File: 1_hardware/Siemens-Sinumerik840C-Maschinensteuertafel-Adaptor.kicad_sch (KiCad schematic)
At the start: 23 parts, among them U1 STM32F103C8T6, U2 AP22652AW6-7, U3 LD1117S33CTR

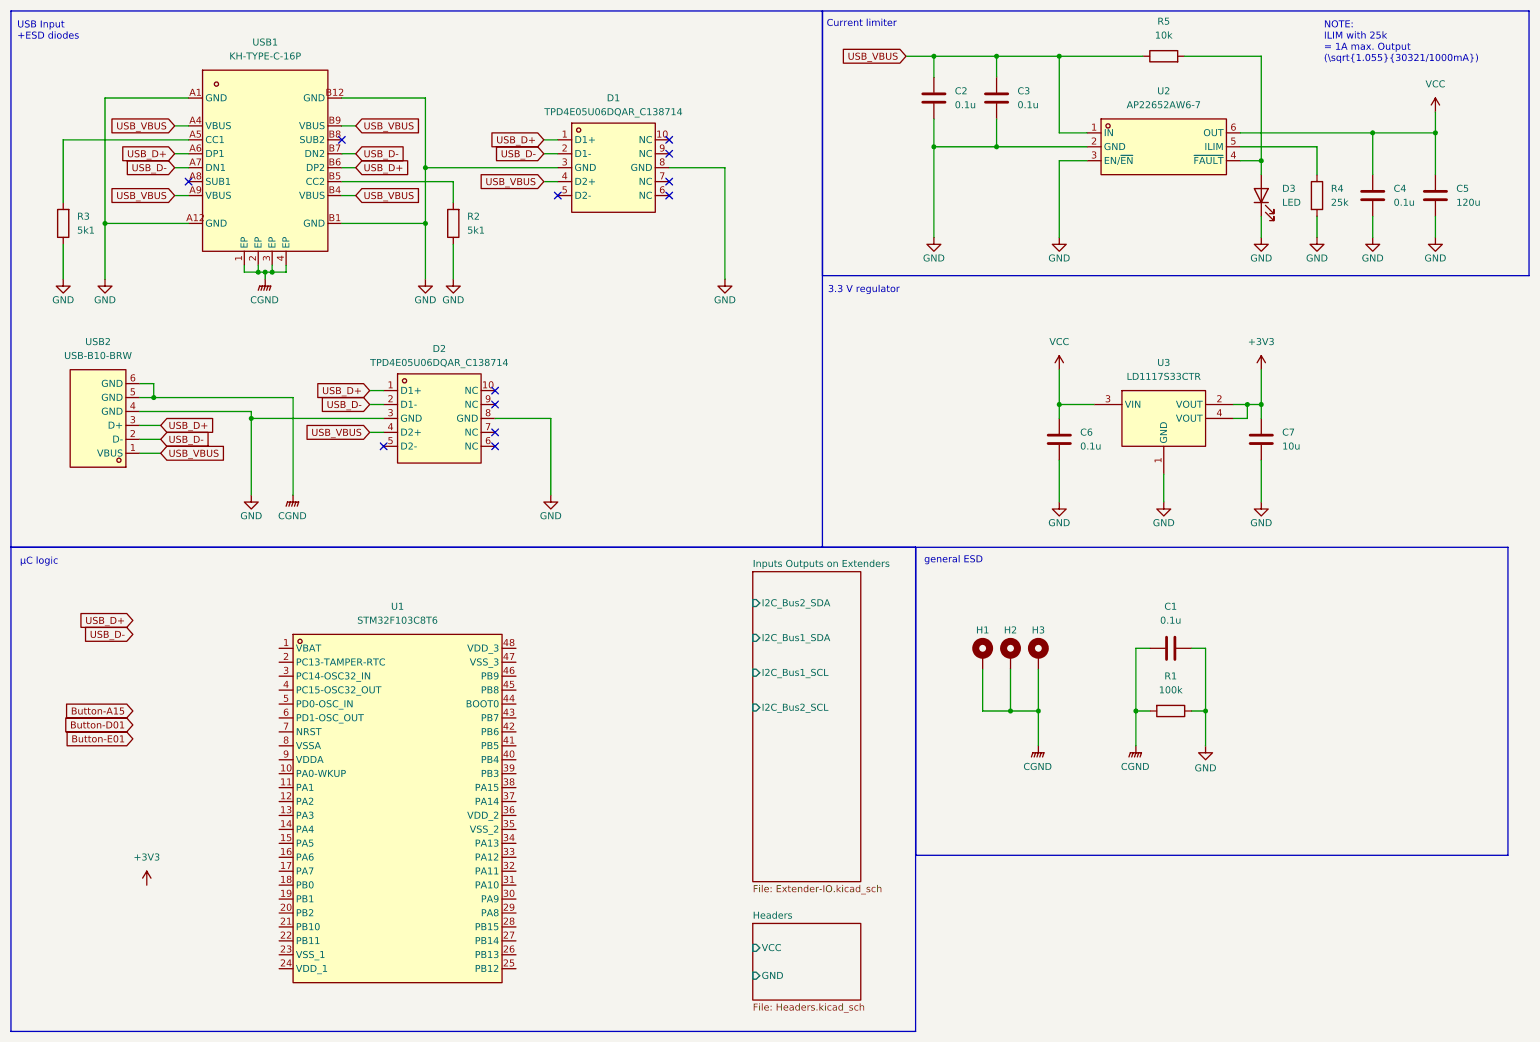
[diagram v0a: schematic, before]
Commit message: finished most of schematic, init STM32 program
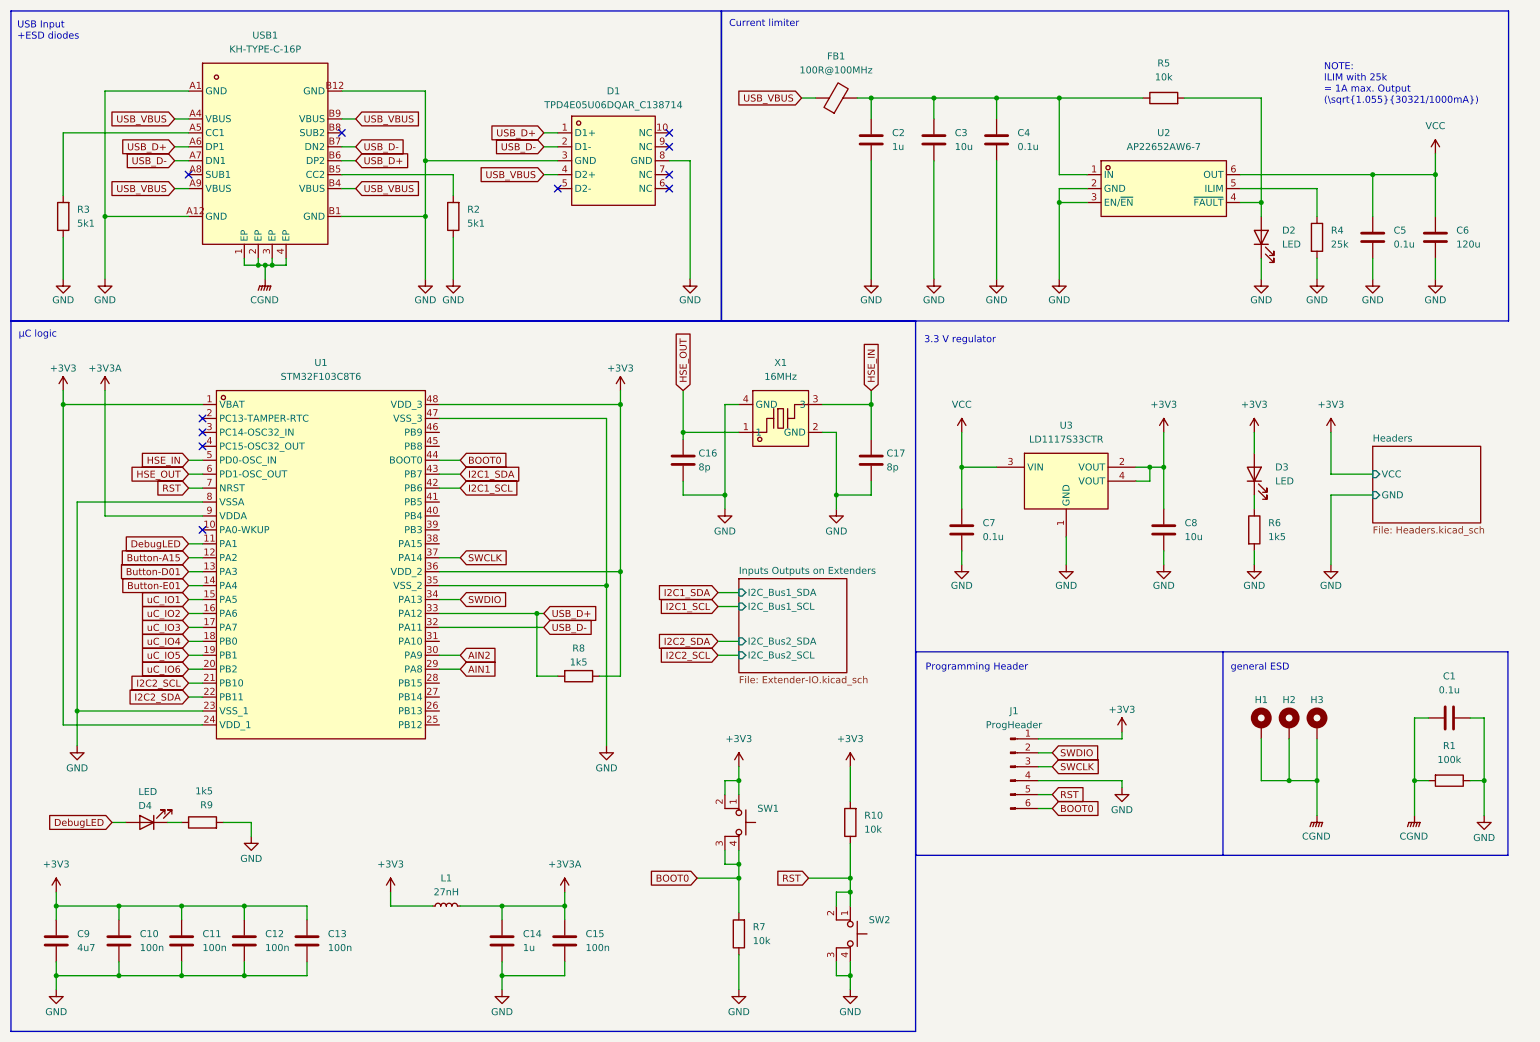
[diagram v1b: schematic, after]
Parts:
- removed D2: TPD4E05U06DQAR_C138714, easyeda2kicad:USON-10_L2.5-W1.0-P0.50-BL, symbol easyeda2kicad:TPD4E05U06DQAR_C138714
- removed USB2: USB-B10-BRW, easyeda2kicad:USB-B-TH_USB-B10-BRW, symbol easyeda2kicad:USB-B10-BRW
- added C10, C11, C12, C13, C15: 100n, Capacitor_SMD:C_0603_1608Metric, symbol Device:C
- added C14, C2: 1u, Capacitor_SMD:C_0603_1608Metric, symbol Device:C
- added C16, C17: 8p, Capacitor_SMD:C_0603_1608Metric, symbol Device:C
- added C9: 4u7, Capacitor_SMD:C_0603_1608Metric, symbol Device:C
- added D3, D4: LED, LED_SMD:LED_0603_1608Metric, symbol Device:LED
- added FB1: 100R@100MHz, easyeda2kicad:L0603, symbol Device:FerriteBead
- added J1: ProgHeader, easyeda2kicad:HDR-SMD_6P-P2.54-V-M-LS4.8_R2, symbol Connector:Conn_01x06_Pin
- added L1: 27nH, Inductor_SMD:L_0603_1608Metric, symbol Device:L_Small
- added R10, R7: 10k, Resistor_SMD:R_0603_1608Metric, symbol Device:R
- added R6, R8, R9: 1k5, Resistor_SMD:R_0603_1608Metric, symbol Device:R
- added SW1, SW2: TS-1187A-B-A-B, easyeda2kicad:SW-SMD_4P-L5.1-W5.1-P3.70-LS6.5-TL-2, symbol Switch:SW_MEC_5E
- added X1: 16MHz, easyeda2kicad:CRYSTAL-SMD_4P-L3.2-W2.5-BL_SIT8008BI, symbol easyeda2kicad:TZ0233A
- C3: renamed from C2; value 0.1u -> 10u
- renumbered C3 to C4, C4 to C5, C5 to C6, C6 to C7, C7 to C8, D3 to D2
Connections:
- net +3V3: now also U1.1 (VBAT), U1.24 (VDD_1), U1.36 (VDD_2), U1.48 (VDD_3), C10.2, C11.2, C12.2, C13.2, C9.2, D3.2 (A), J1.1 (Pin_1), L1.1, R10.2, R8.1, SW1.1, SW1.2
- net Button-A15: now also U1.12 (PA2)
- net Button-D01: now also U1.13 (PA3)
- net Button-E01: now also U1.14 (PA4)
- net GND: now also U1.23 (VSS_1), U1.35 (VSS_2), U1.47 (VSS_3), U1.8 (VSSA), C10.1, C11.1, C12.1, C13.1, C14.1, C15.1, C16.1, C17.1, C2.1, C9.1, J1.4 (Pin_4), R6.2, R7.1, R9.2, SW2.3 (K), SW2.4 (A), X1.2 (GND), X1.4 (GND)
- net USB_D+: now also U1.33 (PA12), R8.2
- net USB_D-: now also U1.32 (PA11)
- net USB_VBUS: now also FB1.1; no longer C3.2, C4.2, R5.1, U2.1 (IN)
- net DebugLED: now reaches U1.11 (PA1)
- net DebugLED: now also D4.2 (A)
- net uC_IO1: now reaches U1.15 (PA5)
- net uC_IO2: now reaches U1.16 (PA6)
- net uC_IO3: now reaches U1.17 (PA7)
- net uC_IO4: now reaches U1.18 (PB0)
- net uC_IO5: now reaches U1.19 (PB1)
- net uC_IO6: now reaches U1.20 (PB2)
- net I2C2_SCL: now reaches U1.21 (PB10)
- net I2C2_SDA: now reaches U1.22 (PB11)
- net AIN1: now reaches U1.29 (PA8)
- net AIN2: now reaches U1.30 (PA9)
- net SWDIO: now reaches U1.34 (PA13)
- net SWDIO: now also J1.2 (Pin_2)
- net SWCLK: now reaches U1.37 (PA14)
- net SWCLK: now also J1.3 (Pin_3)
- net I2C1_SCL: now reaches U1.42 (PB6)
- net I2C1_SDA: now reaches U1.43 (PB7)
- net BOOT0: now reaches U1.44 (BOOT0)
- net BOOT0: now also J1.6 (Pin_6), R7.2, SW1.3 (K), SW1.4 (A)
- net HSE_IN: now reaches U1.5 (PD0-OSC_IN)
- net HSE_IN: now also C17.2, X1.3
- net HSE_OUT: now reaches U1.6 (PD1-OSC_OUT)
- net HSE_OUT: now also C16.2, X1.1
- net RST: now reaches U1.7 (NRST)
- net RST: now also J1.5 (Pin_5), R10.1, SW2.1, SW2.2
- net +3V3A: now reaches U1.9 (VDDA)
- net +3V3A: now also C14.2, C15.2, L1.2
- new net: D3.1 (K), R6.1
- new net: C2.2, C3.2, C4.2, FB1.2, R5.1, U2.1 (IN)
- new net: D4.1 (K), R9.1
- no-connect marks 12 -> 11
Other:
- note added: "Programming Header"
- moved on the sheet: C1, C3, C4, C5, C6, C7, C8, D1, D2, H1, H2, H3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

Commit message: finished schematics and board
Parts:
- added R11, R12, R13, R14, R15, R16, R17, R18: 10k, Resistor_SMD:R_0603_1608Metric, symbol Device:R
- added R19, R20, R21, R22: 1k5, Resistor_SMD:R_0603_1608Metric, symbol Device:R
- C1: footprint Capacitor_SMD:C_0805_2012Metric -> Capacitor_SMD:C_1206_3216Metric
- H1, H2, H3: footprint MountingHole:MountingHole_3.2mm_M3_DIN965_Pad_TopBottom -> MountingHole:MountingHole_3.2mm_M3_DIN965_Pad
- R1: footprint Resistor_SMD:R_0805_2012Metric -> Resistor_SMD:R_1206_3216Metric
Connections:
- net +3V3: now also R11.2, R12.2, R13.2, R14.2, R15.2, R16.2, R17.2, R18.2, R19.2, R20.2, R21.2, R22.2
- net CGND: now also C1.2, H1.1, H2.1, H3.1; no longer C1.1, H1.MP, H2.MP, H3.MP
- net GND: now also C1.1; no longer C1.2
- net I2C1_SCL: now also R20.1
- net I2C1_SDA: now also R19.1
- net I2C2_SCL: now also R22.1
- net I2C2_SDA: now also R21.1
- net USB_D+: now also D1.10 (NC)
- net USB_D-: now also D1.9 (NC)
- net USB_VBUS: now also D1.7 (NC)
- net EXP_INT4: now reaches U1.39 (PB3)
- net EXP_INT4: now also R14.1
- net EXP_INT5: now reaches U1.40 (PB4)
- net EXP_INT5: now also R15.1
- net EXP_INT6: now reaches U1.41 (PB5)
- net EXP_INT6: now also R16.1
- net EXP_INT7: now reaches U1.45 (PB8)
- net EXP_INT7: now also R17.1
- net EXP_INT8: now reaches U1.46 (PB9)
- net EXP_INT8: now also R18.1
- net Button-A15 renamed Button-~{A15}
- net Button-D01 renamed Button-~{D01}
- net Button-E01 renamed Button-~{E01}
- net uC_IO1: no longer names the net of U1.15 (PA5)
- net uC_IO2: no longer names the net of U1.16 (PA6)
- net uC_IO3: no longer names the net of U1.17 (PA7)
- net uC_IO4 renamed EXP_INT1
- net EXP_INT1: now also R11.1
- net uC_IO5 renamed EXP_INT2
- net EXP_INT2: now also R12.1
- net uC_IO6 renamed EXP_INT3
- net EXP_INT3: now also R13.1
- no-connect marks 11 -> 17
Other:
- sheet Inputs Outputs on Extenders renamed IO Expander
- sheet IO Expander ports: added EXP_INT1, EXP_INT2, EXP_INT3, EXP_INT4, EXP_INT5, EXP_INT6, EXP_INT7, EXP_INT8; removed none
- note added: "Programming Header/ Debug"
- note removed: "Programming Header"
- moved on the sheet: C1, C10, C11, C12, C13, C14, C15, C16, C17, C7, C8, C9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

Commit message: changed from STM32F103C8 over to STM32L151C8 changed controller pinout, minor tweaks in board design, added labels and debug pads
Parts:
- removed R8: 1k5, Resistor_SMD:R_0603_1608Metric, symbol Device:R
- removed U1: STM32F103C8T6, easyeda2kicad:LQFP-48_L7.0-W7.0-P0.50-LS9.0-BL, symbol easyeda2kicad:STM32F103C8T6
- added R2: 100k, Resistor_SMD:R_2512_6332Metric, symbol Device:R
- added R23: 1k5, Resistor_SMD:R_0603_1608Metric, symbol Device:R
- added TP1: JTDO-TraceSWO, TestPoint:TestPoint_Pad_D1.0mm, symbol Connector:TestPoint
- added TP2: JTDI, TestPoint:TestPoint_Pad_D1.0mm, symbol Connector:TestPoint
- added TP3: JTCK-SWCLK, TestPoint:TestPoint_Pad_D1.0mm, symbol Connector:TestPoint
- added TP4: JTMS-SWDIO, TestPoint:TestPoint_Pad_D1.0mm, symbol Connector:TestPoint
- added TP5: RESET, TestPoint:TestPoint_Pad_D1.0mm, symbol Connector:TestPoint
- added TP6: GND, TestPoint:TestPoint_Pad_D1.0mm, symbol Connector:TestPoint
- added U1: STM32L151C8T6, easyeda2kicad:LQFP-48_L7.0-W7.0-P0.50-LS9.0-BL, symbol easyeda2kicad:STM32L151C8T6
- C1: footprint Capacitor_SMD:C_1206_3216Metric -> Capacitor_SMD:C_2220_5750Metric
- R1: footprint Resistor_SMD:R_1206_3216Metric -> Resistor_SMD:R_2512_6332Metric
- R10: renamed from R9; value 1k5 -> 470
- R5: value 10k -> 680
- R7: renamed from R6; value 1k5 -> 470
- renumbered R2 to R4, R4 to R6, R7 to R8, R10 to R9
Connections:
- net +3V3: now also R23.1, U1.1 (VLCD), U1.24 (VDD), U1.36 (VDD), U1.48 (VDD)
- net +3V3A: now also U1.9 (VDDA)
- net AIN1: now also U1.11 (PA1)
- net AIN2: now also U1.12 (PA2)
- net BOOT0: now also U1.44 (BOOT0); no longer J1.6 (Pin_6)
- net Button-~{A15}: now also U1.18 (PB0)
- net Button-~{D01}: now also U1.19 (PB1)
- net Button-~{E01}: now also U1.20 (PB2)
- net CGND: now also R2.2
- net DebugLED: now also U1.13 (PA3)
- net EXP_INT1: now also U1.40 (PB4)
- net EXP_INT2: now also U1.41 (PB5)
- net EXP_INT3: now also U1.45 (PB8)
- net EXP_INT4: now also U1.46 (PB9)
- net EXP_INT5: now also U1.25 (PB12)
- net EXP_INT6: now also U1.26 (PB13)
- net EXP_INT7: now also U1.27 (PB14)
- net EXP_INT8: now also U1.28 (PB15)
- net GND: now also R2.1, TP6.1, U1.23 (VSS), U1.35 (VSS), U1.47 (VSS), U1.8 (VSSA)
- net HSE_IN: now also U1.5 (PH0-OSC/IN)
- net HSE_OUT: now also U1.6 (PH1-OSC/OUT)
- net I2C1_SCL: now also U1.42 (PB6)
- net I2C1_SDA: now also U1.43 (PB7)
- net I2C2_SCL: now also U1.21 (PB10)
- net I2C2_SDA: now also U1.22 (PB11)
- net RST: now also TP5.1, U1.7 (NRST)
- net SWCLK: now also TP3.1, U1.37 (PA14)
- net SWDIO: now also TP4.1, U1.34 (PA13)
- net USB_D+: now also R23.2, U1.33 (PA12)
- net USB_D-: now also U1.32 (PA11)
- new net JTDI: TP2.1, U1.38 (PA15)
- new net TSWO: J1.6 (Pin_6), TP1.1, U1.39 (PB3)
- no-connect marks 17 -> 15
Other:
- moved on the sheet: C1, H1, H2, H3, R1, R8, R9, SW1, SW2

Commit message: finished v0.9.2
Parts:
- removed C10, C11, C12, C13, C15: 100n, Capacitor_SMD:C_0603_1608Metric, symbol Device:C
- removed C14: 1u, Capacitor_SMD:C_0603_1608Metric, symbol Device:C
- removed C16, C17: 8p, Capacitor_SMD:C_0603_1608Metric, symbol Device:C
- removed C9: 4u7, Capacitor_SMD:C_0603_1608Metric, symbol Device:C
- removed D4: LED, LED_SMD:LED_0603_1608Metric, symbol Device:LED
- removed J1: ProgHeader, easyeda2kicad:HDR-SMD_6P-P2.54-V-M-LS4.8_R2, symbol Connector:Conn_01x06_Pin
- removed L1: 27nH, Inductor_SMD:L_0603_1608Metric, symbol Device:L_Small
- removed R10: 470, Resistor_SMD:R_0603_1608Metric, symbol Device:R
- removed R11, R12, R13, R14, R15, R16, R17, R18, R8, R9: 10k, Resistor_SMD:R_0603_1608Metric, symbol Device:R
- removed R19, R20, R21, R22, R23: 1k5, Resistor_SMD:R_0603_1608Metric, symbol Device:R
- removed SW1, SW2: TS-1187A-B-A-B, easyeda2kicad:SW-SMD_4P-L5.1-W5.1-P3.70-LS6.5-TL-2, symbol Switch:SW_MEC_5E
- removed TP1: JTDO-TraceSWO, TestPoint:TestPoint_Pad_D1.0mm, symbol Connector:TestPoint
- removed TP2: JTDI, TestPoint:TestPoint_Pad_D1.0mm, symbol Connector:TestPoint
- removed TP3: JTCK-SWCLK, TestPoint:TestPoint_Pad_D1.0mm, symbol Connector:TestPoint
- removed TP4: JTMS-SWDIO, TestPoint:TestPoint_Pad_D1.0mm, symbol Connector:TestPoint
- removed TP5: RESET, TestPoint:TestPoint_Pad_D1.0mm, symbol Connector:TestPoint
- removed TP6: GND, TestPoint:TestPoint_Pad_D1.0mm, symbol Connector:TestPoint
- removed U1: STM32L151C8T6, easyeda2kicad:LQFP-48_L7.0-W7.0-P0.50-LS9.0-BL, symbol easyeda2kicad:STM32L151C8T6
- removed X1: 16MHz, easyeda2kicad:CRYSTAL-SMD_4P-L3.2-W2.5-BL_SIT8008BI, symbol easyeda2kicad:TZ0233A
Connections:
- no-connect marks 15 -> 4
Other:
- removed sheet IO Expander
- added sheet Microcontroller (microcontroller.kicad_sch)
- note added: "Microcontroller"
- note removed: "Programming Header/ Debug"
- note removed: "µC logic"
- moved on the sheet: C1, C2, C3, C4, C5, C6, C7, C8, D1, D2, D3, FB1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

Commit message: pcb v0.9.3 finished
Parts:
- removed C6: 120u, Capacitor_SMD:C_0603_1608Metric, symbol Device:C
- added C6: 100u, Capacitor_SMD:CP_Elec_5x5.8, symbol Device:C_Polarized
- C1: LCSC Part (none) -> C5290327
- R1, R2: LCSC Part (none) -> C25717
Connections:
- net GND: now also C6.2
- net VCC: now also C6.1
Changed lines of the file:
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@@
 		(title "Logic, Power & ESD")
 		(date "2024-10-18")
-		(rev "v0.9.2")
+		(rev "v0.9.3")
 	)
 	(junction
@@
 			)
 		)
+		(property "LCSC Part" " C25717"
+			(at 247.65 124.46 90)
+			(effects
+				(font
+					(size 1.27 1.27)
+				)
+				(hide yes)
+			)
+		)
 		(pin "2"
 		)
@@
 	)
 	(symbol
-		(lib_id "Device:C")
-		(at 152.4 111.76 180)
-		(unit 1)
-		(exclude_from_sim no)
-		(in_bom yes)
-		(on_board yes)
-		(dnp no)
-		(fields_autoplaced yes)
-		(property "Reference" "C6"
-			(at 156.21 110.4899 0)
-			(effects
-				(font
-					(size 1.27 1.27)
-				)
-				(justify right)
-			)
-		)
-		(property "Value" "120u"
-			(at 156.21 113.0299 0)
-			(effects
-				(font
-					(size 1.27 1.27)
-				)
-				(justify right)
-			)
-		)
-		(property "Footprint" "Capacitor_SMD:C_0603_1608Metric"
-			(at 151.4348 107.95 0)
-			(effects
-				(font
-					(size 1.27 1.27)
-				)
-				(hide yes)
-			)
-		)
-		(property "Datasheet" "~"
-			(at 152.4 111.76 0)
-			(effects
-				(font
-					(size 1.27 1.27)
-				)
-				(hide yes)
-			)
-		)
-		(property "Description" "Unpolarized capacitor"
-			(at 152.4 111.76 0)
-			(effects
-				(font
-					(size 1.27 1.27)
-				)
-				(hide yes)
-			)
-		)
-		(pin "1"
-		)
-		(pin "2"
-		)
-		(instances
-			(project "Siemens-Sinumerik840C-Maschinensteuertafel-Adaptor"
-				(path "/82333ccb-6661-4401-8681-de9334259747"
-					(reference "C6")
-					(unit 1)
-				)
-			)
-		)
-	)
-	(symbol
 		(lib_id "power:GND")
 		(at 130.81 176.53 0)
@@
 			)
 		)
+		(property "LCSC Part" " C25717"
+			(at 247.65 134.62 90)
+			(effects
+				(font
+					(size 1.27 1.27)
+				)
+				(hide yes)
+			)
+		)
 		(pin "2"
 		)
@@
 			)
 		)
+		(property "LCSC Part" "C5290327"
+			(at 247.65 113.03 90)
+			(effects
+				(font
+					(size 1.27 1.27)
+				)
+				(hide yes)
+			)
+		)
 		(pin "1"
 		)
@@
 					(unit 1)
 				)
+			)
+		)
+	)
+	(symbol
+		(lib_id "Device:C_Polarized")
+		(at 152.4 111.76 0)
+		(unit 1)
+		(exclude_from_sim no)
+		(in_bom yes)
+		(on_board yes)
+		(dnp no)
+		(property "Reference" "C6"
+			(at 156.21 110.49 0)
+			(effects
+				(font
+					(size 1.27 1.27)
+				)
+				(justify left)
+			)
+		)
+		(property "Value" "100u"
+			(at 156.21 113.03 0)
+			(effects
+				(font
+					(size 1.27 1.27)
+				)
+				(justify left)
+			)
+		)
+		(property "Footprint" "Capacitor_SMD:CP_Elec_5x5.8"
+			(at 153.3652 115.57 0)
+			(effects
+				(font
+					(size 1.27 1.27)
+				)
+				(hide yes)
+			)
+		)
+		(property "Datasheet" "~"
+			(at 152.4 111.76 0)
+			(effects
+				(font
+					(size 1.27 1.27)
+				)
+				(hide yes)
+			)
+		)
+		(property "Description" "tantal capacitor"
+			(at 152.4 111.76 0)
+			(effects
+				(font
+					(size 1.27 1.27)
+				)
+				(hide yes)
+			)
+		)
+		(property "LCSC Part" "C336771"
+			(at 152.4 111.76 0)
+			(effects
+				(font
+					(size 1.27 1.27)
+				)
+				(hide yes)
+			)
+		)
+		(pin "2"
+		)
+		(pin "1"
+		)
+		(instances
+			(project ""
+				(path "/82333ccb-6661-4401-8681-de9334259747"
+					(reference "C6")
+					(unit 1)
+				)

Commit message: PCB v0.9.4 - finished final prototype STM32 project reinitialised (F103C8 -> L151C8)
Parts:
- D1: footprint easyeda2kicad:USON-10_L2.5-W1.0-P0.50-BL -> project_library:USON-10_L2.5-W1.0-P0.50-BL; symbol easyeda2kicad:TPD4E05U06DQAR_C138714 -> project_library:TPD4E05U06DQAR_C138714
- H1, H2, H3: footprint MountingHole:MountingHole_3.2mm_M3_DIN965_Pad -> project_library:MountingHole_3.2mm_M3_DIN965_Pad; symbol Mechanical:MountingHole_Pad_MP -> project_library:MountingHole_Pad_MP_1
- U2: footprint easyeda2kicad:SOT-23-6_L2.9-W1.6-P0.95-LS2.8-BL -> project_library:SOT-23-6_L2.9-W1.6-P0.95-LS2.8-BL; symbol easyeda2kicad:AP22652AW6-7 -> project_library:AP22652AW6-7
- U3: footprint easyeda2kicad:SOT-223-4_L6.5-W3.5-P2.30-LS7.0-BR -> project_library:SOT-223-4_L6.5-W3.5-P2.30-LS7.0-BR; symbol easyeda2kicad:LD1117S33CTR -> project_library:LD1117S33CTR
- USB1: footprint easyeda2kicad:USB-C-SMD_KH-TYPE-C-16P -> project_library:USB-C-SMD_KH-TYPE-C-16P; symbol easyeda2kicad:KH-TYPE-C-16P -> project_library:KH-TYPE-C-16P
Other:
- sheet Headers ports: added none; removed GND, VCC
- moved on the sheet: R3
